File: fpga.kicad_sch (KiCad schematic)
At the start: 52 parts

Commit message: Added i2C level shifter + QSPI Flash to FPGA
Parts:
- removed IC?: PCA9306DCUR, SOP50P310X90-8N, symbol fpga:PCA9306DCUR
- added C?: 100n, symbol Device:C_Small
- added IC?: PCA9306DCUR, SOP50P310X90-8N, symbol fpga:PCA9306DCUR
- added R? (x2): 4.7K, symbol Device:R
- added R?: 0R, symbol Device:R
- added R?: 200k, symbol Device:R
- added X?: ECS-2016MV-500-BN-TR3, Oscillator:Oscillator_DIP-14, symbol Oscillator:ACO-xxxMHz-A
- R? (x2): value 4.7K -> 0R
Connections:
- net QSPI_CS is gone; now on net FLASH_CS: IC?.1 (~{CS}), R?.2
- net +3V3: now also C?.1, IC?.2 (VREF1), R?.1, R?.1, R?.1, X?.14 (Vcc)
- net GND: now also C?.2, IC?.1 (GND), X?.7 (GND)
- net HDMI_5V: now also R?.1
- net HDMI_SCL: now also IC?.6 (SCL2)
- net HDMI_SDA: now also IC?.5 (SDA2)
- net FLASH_CS: now reaches IC?.24 (IO_L01P_2/CSO_B)
- net FLASH_SI: now reaches IC?.27 (IO_L02N_2/MOSI/CSI_B)
- net FLASH_SI: now also IC?.5 (DI_(IO0))
- net FLASH_SO: now reaches IC?.44 (IO_L07N_2/DIN/D0)
- net FLASH_SO: now also IC?.2 (DO_(IO1))
- net FLASH_SCK: now reaches IC?.50 (IO_L09N_2/CCLK)
- net OSC_IN: now reaches IC?.89 (IP_L04N_0/GCLK9)
- net OSC_IN: now also X?.8 (OUT)
- net CCLK renamed FLASH_CLK
- removed net QSPI_DQ0: IC?.2 (DO_(IO1)), IC?.3 (~{WP_(IO2})), IC?.5 (DI_(IO0)), IC?.7 (~{HOLD_(IO3})), R?.1, R?.2
- new net: IC?.3 (~{WP_(IO2})), R?.1
- new net: IC?.7 (VREF2), IC?.8 (EN), R?.2
- new net: R?.2, X?.1 (Tri-State)
- new net: IC?.7 (~{HOLD_(IO3})), R?.2
- new net FPGA_HDMI_SCL: IC?.3 (SCL1), R?.2
- new net FPGA_HDMI_SDA: IC?.4 (SDA1), R?.2
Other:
- note added: "I2C"
- note added: "QSPI FLASH"
- note removed: "I2C - TODO"
- moved on the sheet: C?, IC?, R?

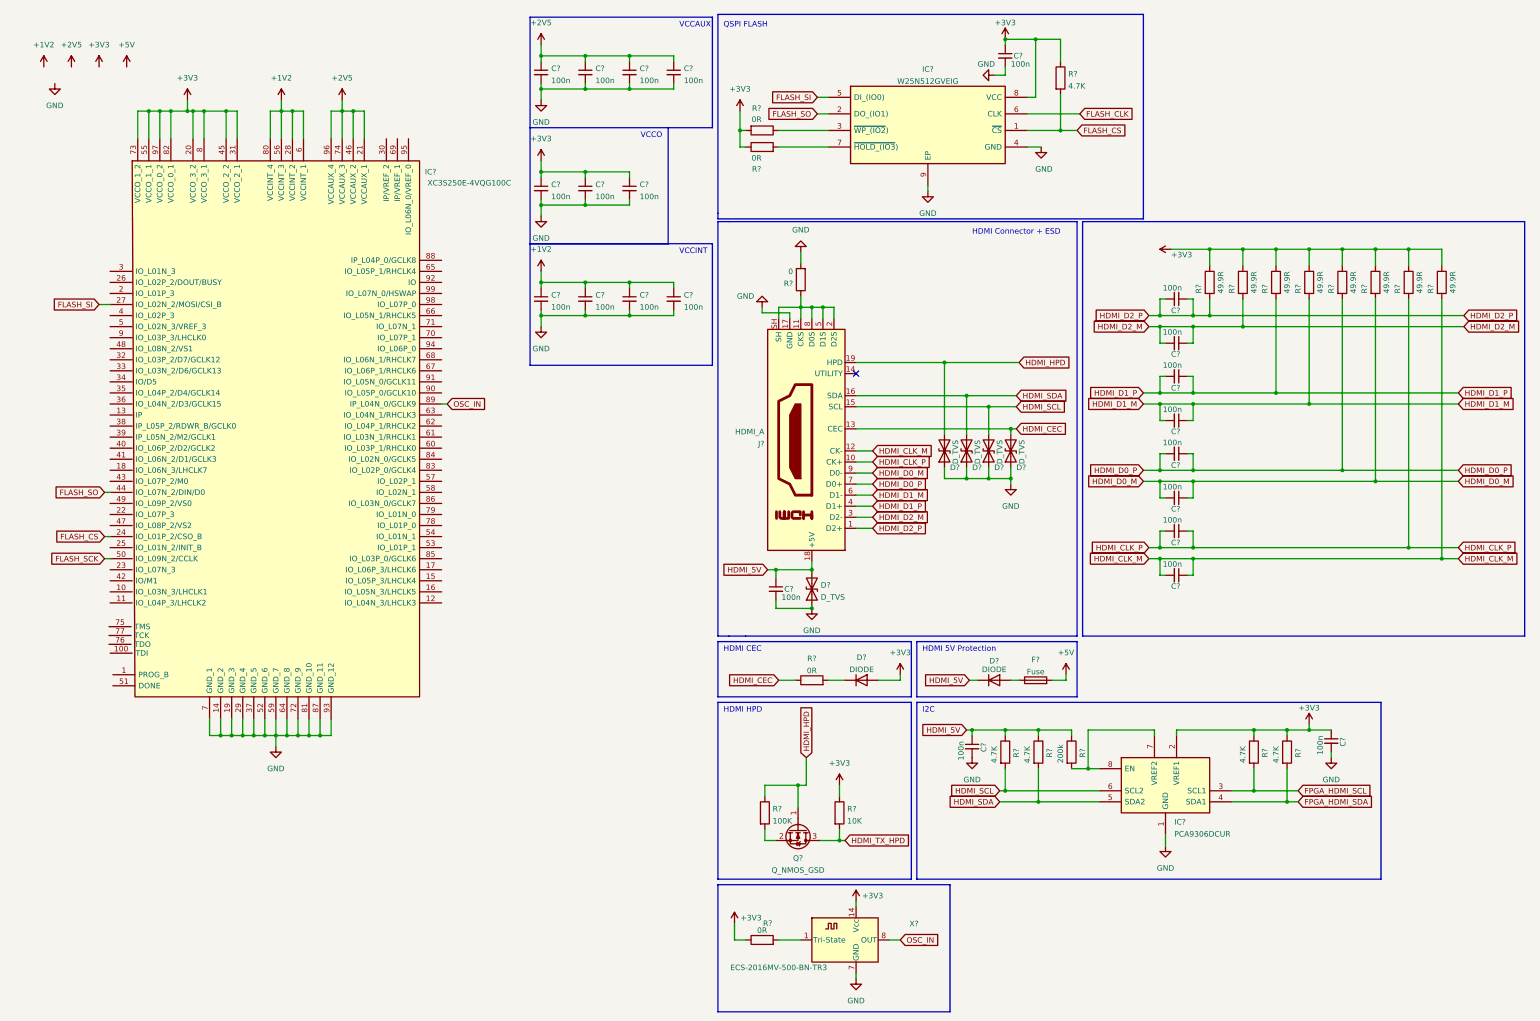
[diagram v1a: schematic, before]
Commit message: Added HDMI connections to fpga
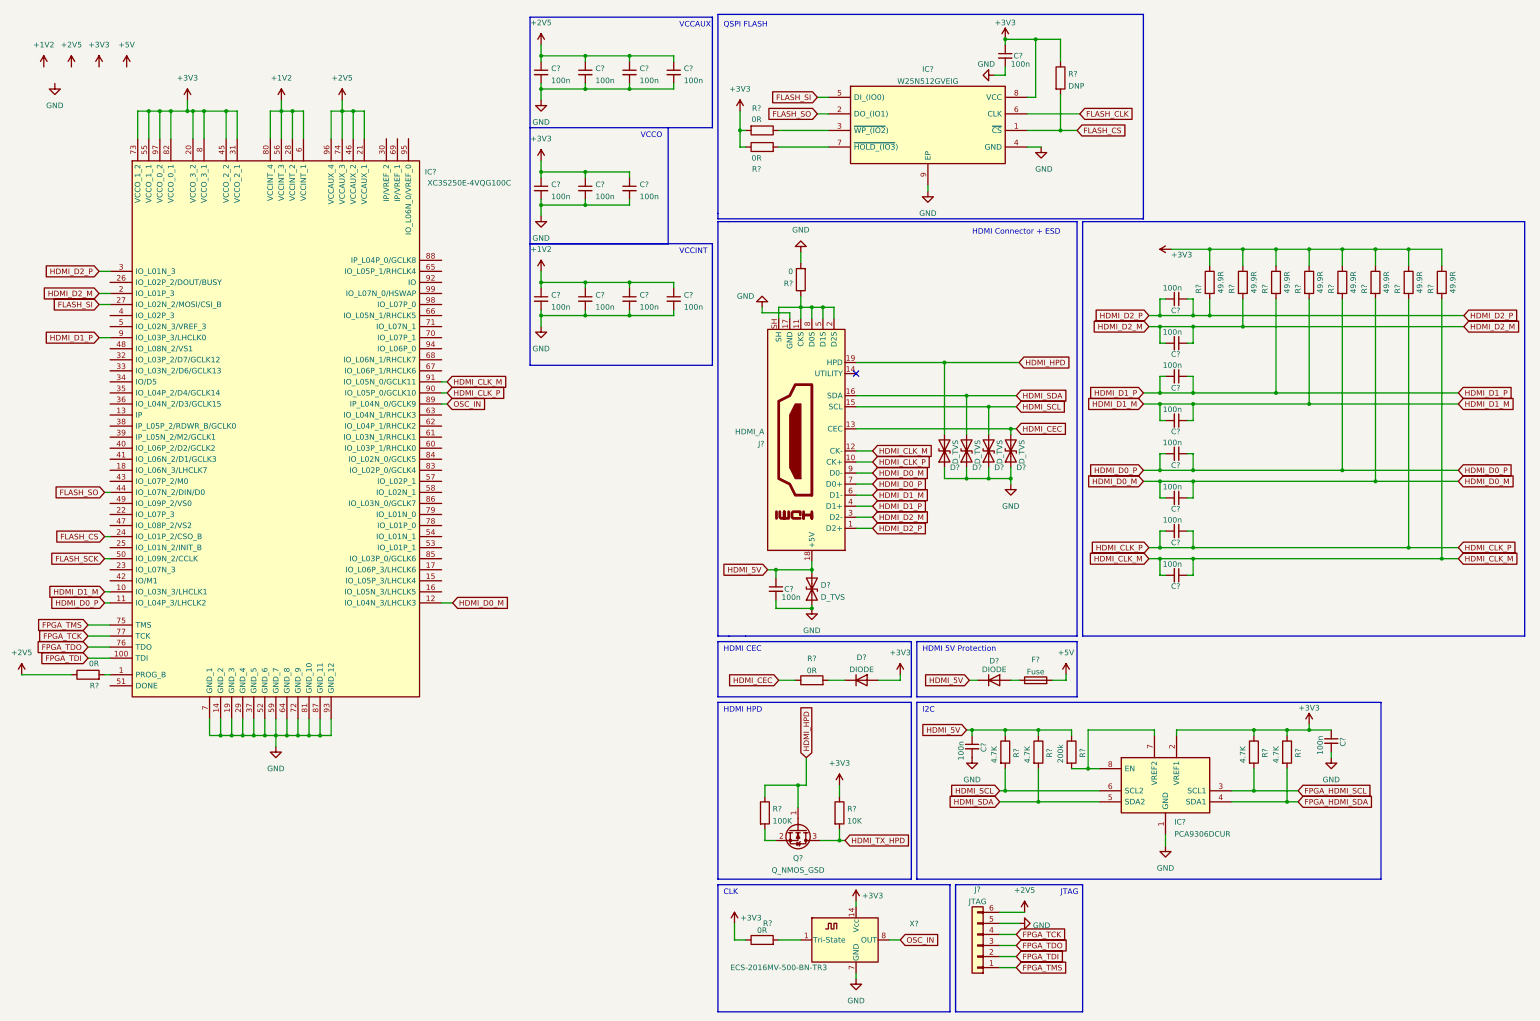
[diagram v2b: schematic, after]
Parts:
- added J?: JTAG, symbol Connector_Generic:Conn_01x06
- added R?: 0R, symbol Device:R
- R?: value 4.7K -> DNP
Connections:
- net +2V5: now also J?.6 (Pin_6), R?.1
- net GND: now also J?.5 (Pin_5)
- net HDMI_CLK_M: now also IC?.91 (IO_L05N_0/GCLK11)
- net HDMI_CLK_P: now also IC?.90 (IO_L05P_0/GCLK10)
- net HDMI_D0_M: now also IC?.12 (IO_L04N_3/LHCLK3)
- net HDMI_D0_P: now also IC?.11 (IO_L04P_3/LHCLK2)
- net HDMI_D1_M: now also IC?.10 (IO_L03N_3/LHCLK1)
- net HDMI_D1_P: now also IC?.9 (IO_L03P_3/LHCLK0)
- net HDMI_D2_M: now also IC?.2 (IO_L01P_3)
- net HDMI_D2_P: now also IC?.3 (IO_L01N_3)
- net at IC?.1 (PROG_B): now also R?.2
- net FPGA_TDI: now reaches IC?.100 (TDI)
- net FPGA_TDI: now also J?.2 (Pin_2)
- net FPGA_TMS: now reaches IC?.75 (TMS)
- net FPGA_TMS: now also J?.1 (Pin_1)
- net FPGA_TDO: now reaches IC?.76 (TDO)
- net FPGA_TDO: now also J?.3 (Pin_3)
- net FPGA_TCK: now reaches IC?.77 (TCK)
- net FPGA_TCK: now also J?.4 (Pin_4)
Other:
- note added: "CLK"
- note added: "JTAG"

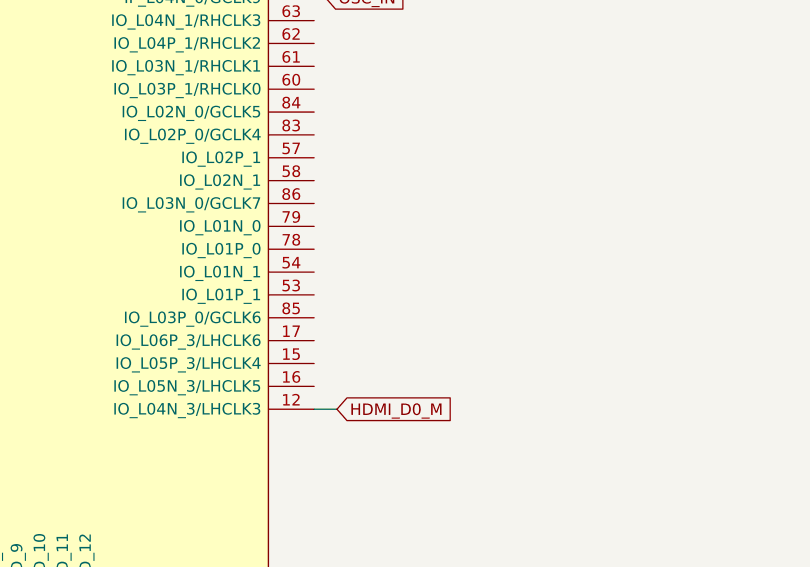
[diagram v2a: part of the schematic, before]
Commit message: Added I2C to fpga
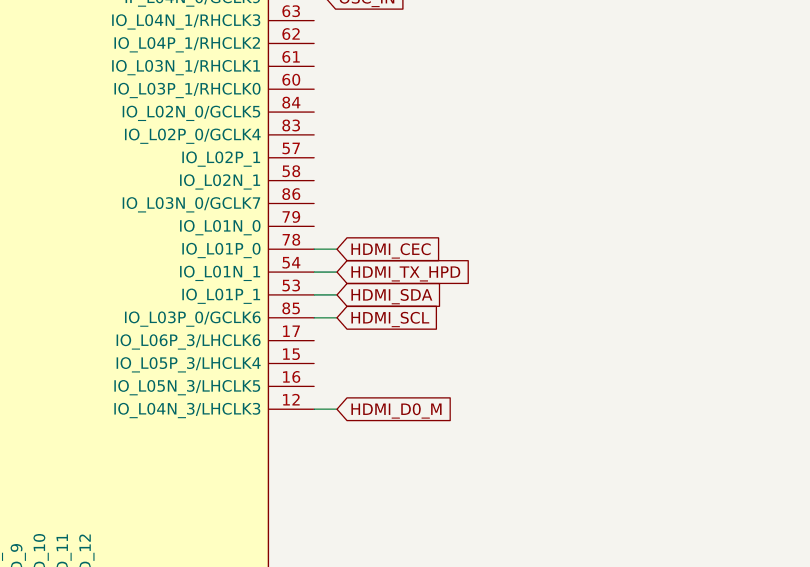
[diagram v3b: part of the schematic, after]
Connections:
- net HDMI_CEC: now also IC?.78 (IO_L01P_0)
- net HDMI_SCL: now also IC?.85 (IO_L03P_0/GCLK6)
- net HDMI_SDA: now also IC?.53 (IO_L01P_1)
- net HDMI_TX_HPD: now also IC?.54 (IO_L01N_1)
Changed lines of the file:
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@@
+    (stroke (width 0) (type default) (color 0 0 0 0))
+  )
+  (wire (pts (xy 113.03 130.81) (xy 115.57 130.81))
     (stroke (width 0) (type default) (color 0 0 0 0))
   )
@@
     (stroke (width 0) (type default) (color 0 0 0 0))
   )
+  (wire (pts (xy 113.03 133.35) (xy 115.57 133.35))
+    (stroke (width 0) (type default) (color 0 0 0 0))
+  )
   (wire (pts (xy 241.3 227.33) (xy 245.11 227.33))
     (stroke (width 0) (type default) (color 0 0 0 0))
@@
     (stroke (width 0) (type default) (color 0 0 0 0))
   )
+  (wire (pts (xy 113.03 135.89) (xy 115.57 135.89))
+    (stroke (width 0) (type default) (color 0 0 0 0))
+  )
   (wire (pts (xy 90.17 33.02) (xy 90.17 35.56))
     (stroke (width 0) (type default) (color 0 0 0 0))
@@
   )
   (wire (pts (xy 304.8 100.33) (xy 346.71 100.33))
+    (stroke (width 0) (type default) (color 0 0 0 0))
+  )
+  (wire (pts (xy 113.03 138.43) (xy 115.57 138.43))
     (stroke (width 0) (type default) (color 0 0 0 0))
   )
@@
     )
   )
+  (global_label "HDMI_SCL" (shape input) (at 115.57 138.43 0) (fields_autoplaced)
+    (effects (font (size 1.27 1.27)) (justify left))
+    (property "Intersheet References" "${INTERSHEET_REFS}" (id 0) (at 127.115 138.5094 0)
+      (effects (font (size 1.27 1.27)) (justify left) hide)
+    )
+  )
   (global_label "HDMI_D1_P" (shape input) (at 34.29 87.63 180) (fields_autoplaced)
     (effects (font (size 1.27 1.27)) (justify right))
@@
     )
   )
+  (global_label "HDMI_TX_HPD" (shape input) (at 115.57 133.35 0) (fields_autoplaced)
+    (effects (font (size 1.27 1.27)) (justify left))
+    (property "Intersheet References" "${INTERSHEET_REFS}" (id 0) (at 130.6226 133.2706 0)
+      (effects (font (size 1.27 1.27)) (justify left) hide)
+    )
+  )
+  (global_label "HDMI_CEC" (shape input) (at 115.57 130.81 0) (fields_autoplaced)
+    (effects (font (size 1.27 1.27)) (justify left))
+    (property "Intersheet References" "${INTERSHEET_REFS}" (id 0) (at 127.2964 130.8894 0)
+      (effects (font (size 1.27 1.27)) (justify left) hide)
+    )
+  )
   (global_label "HDMI_5V" (shape input) (at 233.68 177.8 180) (fields_autoplaced)
     (effects (font (size 1.27 1.27)) (justify right))
@@
       (effects (font (size 1.27 1.27)) (justify left) hide)
     )
+  )
+  (global_label "HDMI_SDA" (shape input) (at 115.57 135.89 0) (fields_autoplaced)
+    (effects (font (size 1.27 1.27)) (justify left))
+    (property "Intersheet References" "${INTERSHEET_REFS}" (id 0) (at 127.1755 135.9694 0)
+      (effects (font (size 1.27 1.27)) (justify left) hide)
+    )
